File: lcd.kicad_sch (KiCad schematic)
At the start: 2 parts, among them J1 687110149022, J2 687140149022

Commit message: Continue schematic review
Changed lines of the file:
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@@
 	(text "TFT LCD 40 pins driver connector"
 		(exclude_from_sim no)
-		(at 95.758 36.322 0)
+		(at 95.25 36.83 0)
 		(effects
 			(font
@@
 	(text "TFT LCD 10 pins touch connector"
 		(exclude_from_sim no)
-		(at 168.148 67.056 0)
+		(at 167.64 67.31 0)
 		(effects
 			(font
@@
 	(text "TFT LCD screen"
 		(exclude_from_sim no)
-		(at 149.352 24.638 0)
+		(at 149.86 24.13 0)
 		(effects
 			(font

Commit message: Add TODOs and update pdf schematic
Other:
- note added: "TODO: think about ferrite beam on LCD connectors"
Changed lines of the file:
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@@
+		)
+	)
+	(text "TODO: think about ferrite beam on LCD connectors"
+		(exclude_from_sim no)
+		(at 170.434 116.332 0)
+		(effects
+			(font
+				(size 1.27 1.27)
+			)
 		)
 	)

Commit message: Fix some little warnings and refomat schematics files
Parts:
- renumbered J2 to J6, J1 to J7
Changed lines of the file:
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@@
 		(dnp no)
 		(fields_autoplaced yes)
-		(property "Reference" "#PWR015"
+		(property "Reference" "#PWR0126"
 			(at 124.46 119.38 0)
 			(effects
@@
 			(project "weather-station-poc"
 				(path "/38eb53bb-294e-46e4-ad59-fd355ca373b9/887aec76-5086-421b-8a43-0ed64a6cc9fd"
-					(reference "#PWR015")
+					(reference "#PWR0126")
 					(unit 1)
 				)
@@
 		(dnp no)
 		(fields_autoplaced yes)
-		(property "Reference" "#PWR025"
+		(property "Reference" "#PWR0123"
 			(at 86.36 48.26 0)
 			(effects
@@
 			(project "weather-station-poc"
 				(path "/38eb53bb-294e-46e4-ad59-fd355ca373b9/887aec76-5086-421b-8a43-0ed64a6cc9fd"
-					(reference "#PWR025")
+					(reference "#PWR0123")
 					(unit 1)
 				)
@@
 		(dnp no)
 		(fields_autoplaced yes)
-		(property "Reference" "#PWR016"
+		(property "Reference" "#PWR0127"
 			(at 124.46 137.16 0)
 			(effects
@@
 			(project "weather-station-poc"
 				(path "/38eb53bb-294e-46e4-ad59-fd355ca373b9/887aec76-5086-421b-8a43-0ed64a6cc9fd"
-					(reference "#PWR016")
+					(reference "#PWR0127")
 					(unit 1)
 				)
@@
 		(dnp no)
 		(fields_autoplaced yes)
-		(property "Reference" "#PWR027"
+		(property "Reference" "#PWR0128"
 			(at 158.75 78.74 0)
 			(effects
@@
 			(project "weather-station-poc"
 				(path "/38eb53bb-294e-46e4-ad59-fd355ca373b9/887aec76-5086-421b-8a43-0ed64a6cc9fd"
-					(reference "#PWR027")
+					(reference "#PWR0128")
 					(unit 1)
 				)
@@
 		(dnp no)
 		(fields_autoplaced yes)
-		(property "Reference" "#PWR028"
+		(property "Reference" "#PWR0129"
 			(at 158.75 81.28 0)
 			(effects
@@
 			(project "weather-station-poc"
 				(path "/38eb53bb-294e-46e4-ad59-fd355ca373b9/887aec76-5086-421b-8a43-0ed64a6cc9fd"
-					(reference "#PWR028")
+					(reference "#PWR0129")
 					(unit 1)
 				)
@@
 		(dnp no)
 		(fields_autoplaced yes)
-		(property "Reference" "#PWR026"
+		(property "Reference" "#PWR0124"
 			(at 86.36 50.8 0)
 			(effects
@@
 			(project "weather-station-poc"
 				(path "/38eb53bb-294e-46e4-ad59-fd355ca373b9/887aec76-5086-421b-8a43-0ed64a6cc9fd"
-					(reference "#PWR026")
+					(reference "#PWR0124")
 					(unit 1)
 				)
@@
 		(dnp no)
 		(fields_autoplaced yes)
-		(property "Reference" "#PWR023"
+		(property "Reference" "#PWR0130"
 			(at 196.85 78.74 0)
 			(effects
@@
 			(project "weather-station-poc"
 				(path "/38eb53bb-294e-46e4-ad59-fd355ca373b9/887aec76-5086-421b-8a43-0ed64a6cc9fd"
-					(reference "#PWR023")
+					(reference "#PWR0130")
 					(unit 1)
 				)
@@
 		(dnp no)
 		(fields_autoplaced yes)
-		(property "Reference" "J2"
+		(property "Reference" "J6"
 			(at 105.41 40.64 0)
 			(effects
@@
 			(project ""
 				(path "/38eb53bb-294e-46e4-ad59-fd355ca373b9/887aec76-5086-421b-8a43-0ed64a6cc9fd"
-					(reference "J2")
+					(reference "J6")
 					(unit 1)
 				)
@@
 		(dnp no)
 		(fields_autoplaced yes)
-		(property "Reference" "#PWR014"
+		(property "Reference" "#PWR0125"
 			(at 124.46 53.34 0)
 			(effects
@@
 			(project ""
 				(path "/38eb53bb-294e-46e4-ad59-fd355ca373b9/887aec76-5086-421b-8a43-0ed64a6cc9fd"
-					(reference "#PWR014")
+					(reference "#PWR0125")
 					(unit 1)
 				)
@@
 		(dnp no)
 		(fields_autoplaced yes)
-		(property "Reference" "J1"
+		(property "Reference" "J7"
 			(at 177.8 71.12 0)
 			(effects
@@
 			(project ""
 				(path "/38eb53bb-294e-46e4-ad59-fd355ca373b9/887aec76-5086-421b-8a43-0ed64a6cc9fd"
-					(reference "J1")
+					(reference "J7")
 					(unit 1)
 				)
@@
 		(dnp no)
 		(fields_autoplaced yes)
-		(property "Reference" "#PWR024"
+		(property "Reference" "#PWR0131"
 			(at 196.85 88.9 0)
 			(effects
@@
 			(project "weather-station-poc"
 				(path "/38eb53bb-294e-46e4-ad59-fd355ca373b9/887aec76-5086-421b-8a43-0ed64a6cc9fd"
-					(reference "#PWR024")
-					(unit 1)
-				)
+					(reference "#PWR0131")
+					(unit 1)
+				)

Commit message: Fill the cartridge for all schematics
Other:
- company: (none) -> Julien Cruvieux
- title: (none) -> LCD
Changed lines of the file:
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@@
 	(generator_version "9.0")
 	(paper "A4")
+	(title_block
+		(title "LCD")
+		(date "2025-12-26")
+		(rev "A")
+		(company "Julien Cruvieux")
+	)
 	(rectangle
 		(start 83.82 38.1)

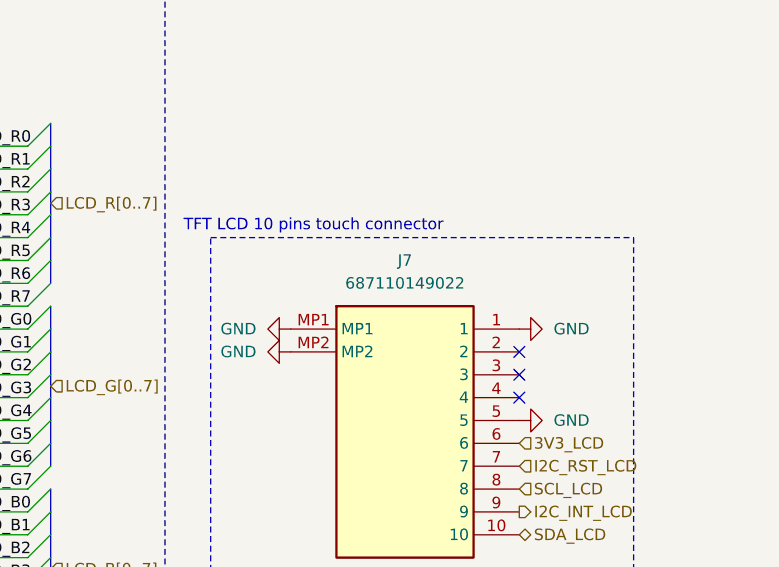
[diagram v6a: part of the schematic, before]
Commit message: LCD 10 pins connector is top and not bottom face, replace connector part
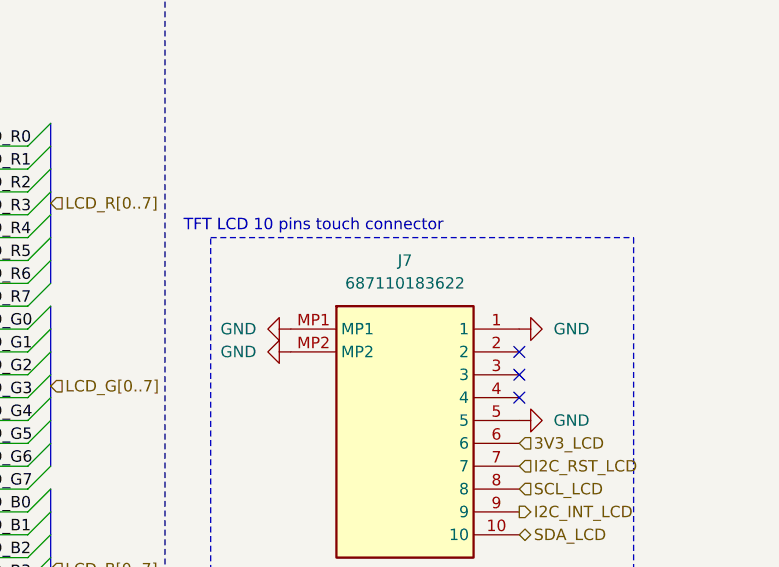
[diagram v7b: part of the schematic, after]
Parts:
- removed J7: 687110149022, weather-station-poc-fp:687110149022, symbol weather-station-poc-sym:687110149022
- added J7: 687110183622, weather-station-poc-fp:687110183622, symbol weather-station-poc-sym:687110183622
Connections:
- net 3V3_LCD: now also J7.6
- net GND: now also J7.1, J7.5, J7.MP1, J7.MP2
- net I2C_INT_LCD: now also J7.9
- net I2C_RST_LCD: now also J7.7
- net SCL_LCD: now also J7.8
- net SDA_LCD: now also J7.10
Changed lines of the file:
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@@
-	)
-	(symbol
-		(lib_id "weather-station-poc-sym:687110149022")
-		(at 165.1 78.74 0)
-		(unit 1)
-		(exclude_from_sim no)
-		(in_bom yes)
-		(on_board yes)
-		(dnp no)
-		(fields_autoplaced yes)
-		(property "Reference" "J7"
-			(at 177.8 71.12 0)
-			(effects
-				(font
-					(size 1.27 1.27)
-				)
-			)
-		)
-		(property "Value" "687110149022"
-			(at 177.8 73.66 0)
-			(effects
-				(font
-					(size 1.27 1.27)
-				)
-			)
-		)
-		(property "Footprint" "weather-station-poc-fp:687110149022"
-			(at 186.69 173.66 0)
-			(effects
-				(font
-					(size 1.27 1.27)
-				)
-				(justify left top)
-				(hide yes)
-			)
-		)
-		(property "Datasheet" "https://www.we-online.com/components/products/download/687110149022+%28rev1%29.pdf"
-			(at 186.69 273.66 0)
-			(effects
-				(font
-					(size 1.27 1.27)
-				)
-				(justify left top)
-				(hide yes)
-			)
-		)
-		(property "Description" "WR-FPC 0.50mm SMT Horiz. Bot. Contact Hinge type WR-FPC 0.50mm 10pins Hinge type SMT Horizontal Bottom Contact"
-			(at 165.1 78.74 0)
-			(effects
-				(font
-					(size 1.27 1.27)
-				)
-				(hide yes)
-			)
-		)
-		(property "Height" "2.3"
-			(at 186.69 473.66 0)
-			(effects
-				(font
-					(size 1.27 1.27)
-				)
-				(justify left top)
-				(hide yes)
-			)
-		)
-		(property "Mouser Part Number" "710-687110149022"
-			(at 186.69 573.66 0)
-			(effects
-				(font
-					(size 1.27 1.27)
-				)
-				(justify left top)
-				(hide yes)
-			)
-		)
-		(property "Mouser Price/Stock" "https://www.mouser.co.uk/ProductDetail/Wurth-Elektronik/687110149022?qs=a9WhcLg8qCyH8vExLXgvKQ%3D%3D"
-			(at 186.69 673.66 0)
-			(effects
-				(font
-					(size 1.27 1.27)
-				)
-				(justify left top)
-				(hide yes)
-			)
-		)
-		(property "Manufacturer_Name" "Wurth Elektronik"
-			(at 186.69 773.66 0)
-			(effects
-				(font
-					(size 1.27 1.27)
-				)
-				(justify left top)
-				(hide yes)
-			)
-		)
-		(property "Manufacturer_Part_Number" "687110149022"
-			(at 186.69 873.66 0)
-			(effects
-				(font
-					(size 1.27 1.27)
-				)
-				(justify left top)
-				(hide yes)
-			)
-		)
-		(pin "MP2"
-		)
-		(pin "8"
-		)
-		(pin "MP1"
-		)
-		(pin "10"
-		)
-		(pin "1"
-		)
-		(pin "4"
-		)
-		(pin "6"
-		)
-		(pin "7"
-		)
-		(pin "5"
-		)
-		(pin "2"
-		)
-		(pin "3"
-		)
-		(pin "9"
-		)
-		(instances
-			(project ""
-				(path "/38eb53bb-294e-46e4-ad59-fd355ca373b9/887aec76-5086-421b-8a43-0ed64a6cc9fd"
-					(reference "J7")
-					(unit 1)
-				)
-			)
-		)
 	)
 	(symbol
@@
 					(unit 1)
 				)
+			)
+		)
+	)
+	(symbol
+		(lib_id "weather-station-poc-sym:687110183622")
+		(at 165.1 78.74 0)
+		(unit 1)
+		(exclude_from_sim no)
+		(in_bom yes)
+		(on_board yes)
+		(dnp no)
+		(fields_autoplaced yes)
+		(property "Reference" "J7"
+			(at 177.8 71.12 0)
+			(effects
+				(font
+					(size 1.27 1.27)
+				)
+			)
+		)
+		(property "Value" "687110183622"
+			(at 177.8 73.66 0)
+			(effects
+				(font
+					(size 1.27 1.27)
+				)
+			)
+		)
+		(property "Footprint" "weather-station-poc-fp:687110183622"
+			(at 186.69 173.66 0)
+			(effects
+				(font
+					(size 1.27 1.27)
+				)
+				(justify left top)
+				(hide yes)
+			)
+		)
+		(property "Datasheet" "https://www.we-online.com/components/products/download/687110183622+%28rev1%29.pdf"
+			(at 186.69 273.66 0)
+			(effects
+				(font
+					(size 1.27 1.27)
+				)
+				(justify left top)
+				(hide yes)
+			)
+		)
+		(property "Description" "WR-FPC 0.50mm SMT Horiz. Top Cont. Low Profile WR-FPC 0.50mm 10pins low profile SMT Horizontal Top Contact"
+			(at 165.1 78.74 0)
+			(effects
+				(font
+					(size 1.27 1.27)
+				)
+				(hide yes)
+			)
+		)
+		(property "Height" "1.3"
+			(at 186.69 473.66 0)
+			(effects
+				(font
+					(size 1.27 1.27)
+				)
+				(justify left top)
+				(hide yes)
+			)
+		)
+		(property "Mouser Part Number" "710-687110183622"
+			(at 186.69 573.66 0)
+			(effects
+				(font
+					(size 1.27 1.27)
+				)
+				(justify left top)
+				(hide yes)
+			)
+		)
+		(property "Mouser Price/Stock" "https://www.mouser.co.uk/ProductDetail/Wurth-Elektronik/687110183622?qs=5aG0NVq1C4xCi7o2O%2FGa6w%3D%3D"
+			(at 186.69 673.66 0)
+			(effects
+				(font
+					(size 1.27 1.27)
+				)
+				(justify left top)
+				(hide yes)
+			)
+		)
+		(property "Manufacturer_Name" "Wurth Elektronik"
+			(at 186.69 773.66 0)
+			(effects
+				(font
+					(size 1.27 1.27)
+				)
+				(justify left top)
+				(hide yes)
+			)
+		)
+		(property "Manufacturer_Part_Number" "687110183622"
+			(at 186.69 873.66 0)
+			(effects
+				(font
+					(size 1.27 1.27)
+				)
+				(justify left top)
+				(hide yes)
+			)
+		)
+		(pin "5"
+		)
+		(pin "6"
+		)
+		(pin "10"
+		)
+		(pin "4"
+		)
+		(pin "1"
+		)
+		(pin "3"
+		)
+		(pin "7"
+		)
+		(pin "8"
+		)
+		(pin "MP2"
+		)
+		(pin "MP1"
+		)
+		(pin "9"
+		)
+		(pin "2"
+		)
+		(instances
+			(project ""
+				(path "/38eb53bb-294e-46e4-ad59-fd355ca373b9/887aec76-5086-421b-8a43-0ed64a6cc9fd"
+					(reference "J7")
+					(unit 1)
+				)
